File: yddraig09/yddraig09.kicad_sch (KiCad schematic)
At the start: 6 parts

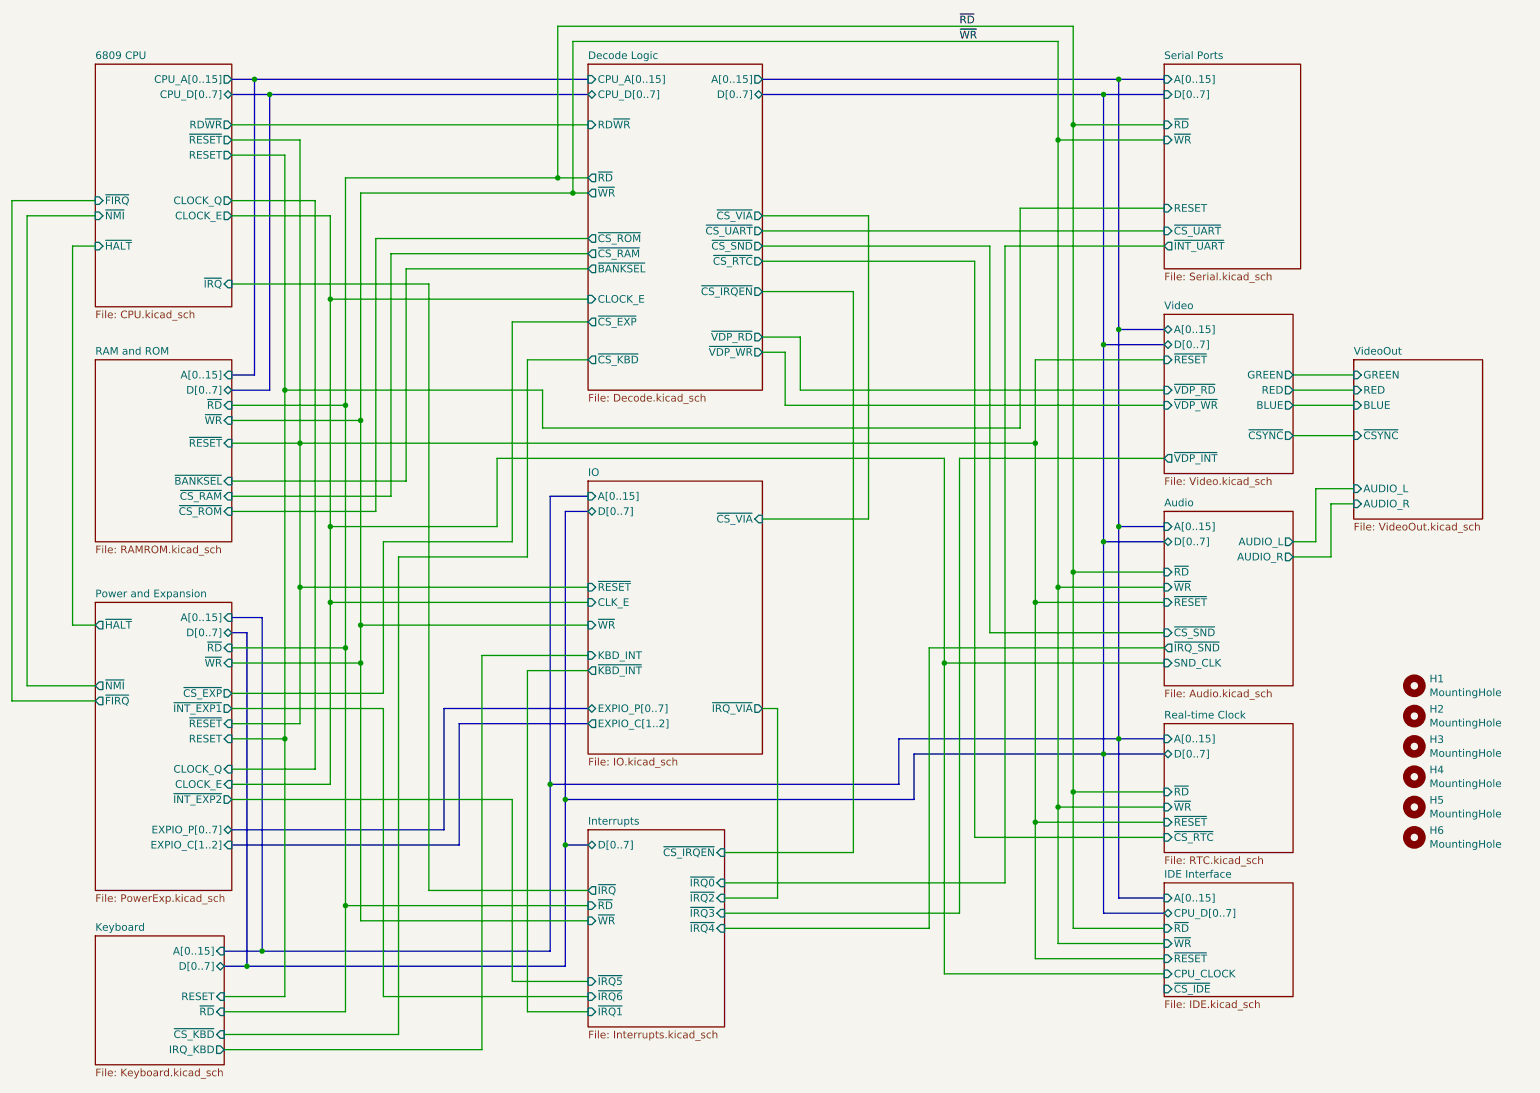
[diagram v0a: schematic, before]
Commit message: Finished changes to 6809 schematics
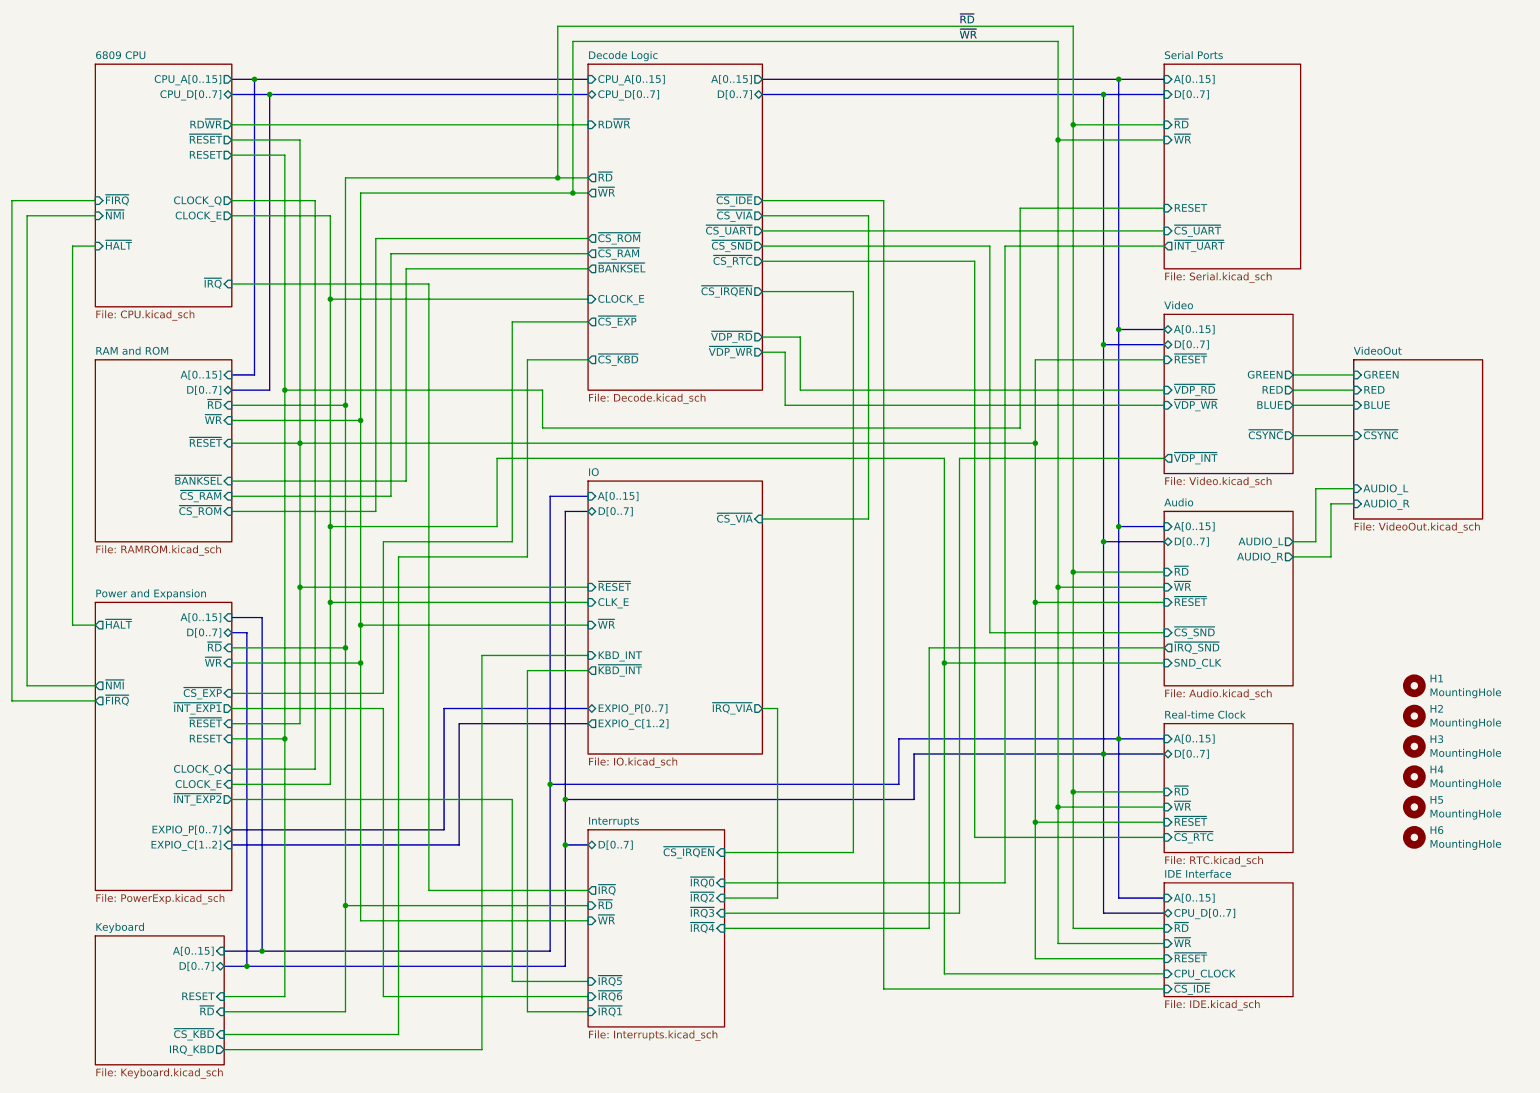
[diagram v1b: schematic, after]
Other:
- sheet Decode Logic ports: added ~{CS_IDE}; removed none
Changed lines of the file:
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@@
 	(wire
 		(pts
+			(xy 152.4 44.45) (xy 172.72 44.45)
+		)
+		(stroke
+			(width 0)
+			(type default)
+		)
+	)
+	(wire
+		(pts
 			(xy 198.12 85.09) (xy 198.12 71.12)
 		)
@@
 		)
 	)
+	(wire
+		(pts
+			(xy 172.72 176.53) (xy 219.71 176.53)
+		)
+		(stroke
+			(width 0)
+			(type default)
+		)
+	)
 	(bus
 		(pts
@@
 	(wire
 		(pts
+			(xy 170.18 46.99) (xy 170.18 97.79)
+		)
+		(stroke
+			(width 0)
+			(type default)
+		)
+	)
+	(wire
+		(pts
 			(xy 74.93 132.08) (xy 63.5 132.08)
 		)
@@
 		)
 	)
-	(bus
+	(wire
 		(pts
-			(xy 69.85 76.2) (xy 69.85 26.67)
+			(xy 172.72 44.45) (xy 172.72 176.53)
 		)
 		(stroke
@@
 	(bus
 		(pts
-			(xy 123.19 26.67) (xy 69.85 26.67)
+			(xy 69.85 76.2) (xy 69.85 26.67)
 		)
 		(stroke
@@
 		)
 	)
-	(wire
+	(bus
 		(pts
-			(xy 198.12 148.59) (xy 198.12 171.45)
+			(xy 123.19 26.67) (xy 69.85 26.67)
 		)
 		(stroke
@@
 	(wire
 		(pts
-			(xy 80.01 60.96) (xy 123.19 60.96)
+			(xy 198.12 148.59) (xy 198.12 171.45)
 		)
 		(stroke
@@
 	(wire
 		(pts
-			(xy 198.12 85.09) (xy 198.12 111.76)
+			(xy 80.01 60.96) (xy 123.19 60.96)
 		)
 		(stroke
@@
 	(wire
 		(pts
-			(xy 219.71 109.22) (xy 201.93 109.22)
+			(xy 198.12 85.09) (xy 198.12 111.76)
 		)
 		(stroke
@@
 	(wire
 		(pts
-			(xy 170.18 46.99) (xy 170.18 97.79)
+			(xy 219.71 109.22) (xy 201.93 109.22)
 		)
 		(stroke
@@
 			)
 		)
-		(property "Description" ""
+		(property "Description" "Mounting Hole without connection"
 			(at 261.62 140.97 0)
 			(effects
@@
 			)
 		)
-		(property "Description" ""
+		(property "Description" "Mounting Hole without connection"
 			(at 261.62 130.81 0)
 			(effects
@@
 			)
 		)
-		(property "Description" ""
+		(property "Description" "Mounting Hole without connection"
 			(at 261.62 125.73 0)
 			(effects
@@
 			)
 		)
-		(property "Description" ""
+		(property "Description" "Mounting Hole without connection"
 			(at 261.62 146.05 0)
 			(effects
@@
 			)
 		)
-		(property "Description" ""
+		(property "Description" "Mounting Hole without connection"
 			(at 261.62 151.13 0)
 			(effects
@@
 			)
 		)
-		(property "Description" ""
+		(property "Description" "Mounting Hole without connection"
 			(at 261.62 135.89 0)
 			(effects
@@
 			)
 		)
+		(pin "~{CS_IDE}" output
+			(at 152.4 44.45 0)
+			(effects
+				(font
+					(size 1.27 1.27)
+				)
+				(justify right)
+			)
+		)
 		(instances
 			(project "yddraig09"
@@
 			)
 		)
-		(pin "~{CS_EXP}" output
-			(at 63.5 127 0)
-			(effects
-				(font
-					(size 1.27 1.27)
-				)
-				(justify right)
-			)
-		)
 		(pin "D[0..7]" bidirectional
 			(at 63.5 116.84 0)
@@
 			(effects
 				(font
+					(size 1.27 1.27)
+				)
+				(justify right)
+			)
+		)
+		(pin "~{CS_EXP}" input
+			(at 63.5 127 0)
+			(effects
+				(font

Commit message: Changes to yddraig09
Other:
- sheet RAM and ROM ports: added CPU_A[0..15], CPU_D[0..7]; removed A[0..15], D[0..7]
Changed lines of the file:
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@@
 			)
 		)
-		(pin "A[0..15]" input
-			(at 63.5 73.66 0)
+		(pin "CPU_D[0..7]" bidirectional
+			(at 63.5 76.2 0)
 			(effects
 				(font
@@
 			)
 		)
-		(pin "D[0..7]" bidirectional
-			(at 63.5 76.2 0)
+		(pin "CPU_A[0..15]" input
+			(at 63.5 73.66 0)
 			(effects
 				(font

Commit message: BOard changes
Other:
- removed sheet Real-time Clock
- sheet Decode Logic ports: added none; removed ~{CS_RTC}
- sheet IO ports: added EXPIO_P[0..5], SCL, SDA, ~{FIFO_EMPTY}; removed EXPIO_P[0..7], KBD_INT
- sheet Keyboard ports: added ~{FIFO_EMPTY}; removed IRQ_KBD
- sheet Power and Expansion ports: added EXPIO_P[0..5], SCL, SDA; removed EXPIO_P[0..7]
